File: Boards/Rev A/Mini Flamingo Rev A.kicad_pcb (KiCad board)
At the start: 2 copper layers, 38.1 x 25.4 mm, 23 parts, among them J1 ISP_Header, J2 APA102C Out, J3 Batt Conn, SW1 Power Switch, U1 ATTINY85-20SU, U2 APA102C

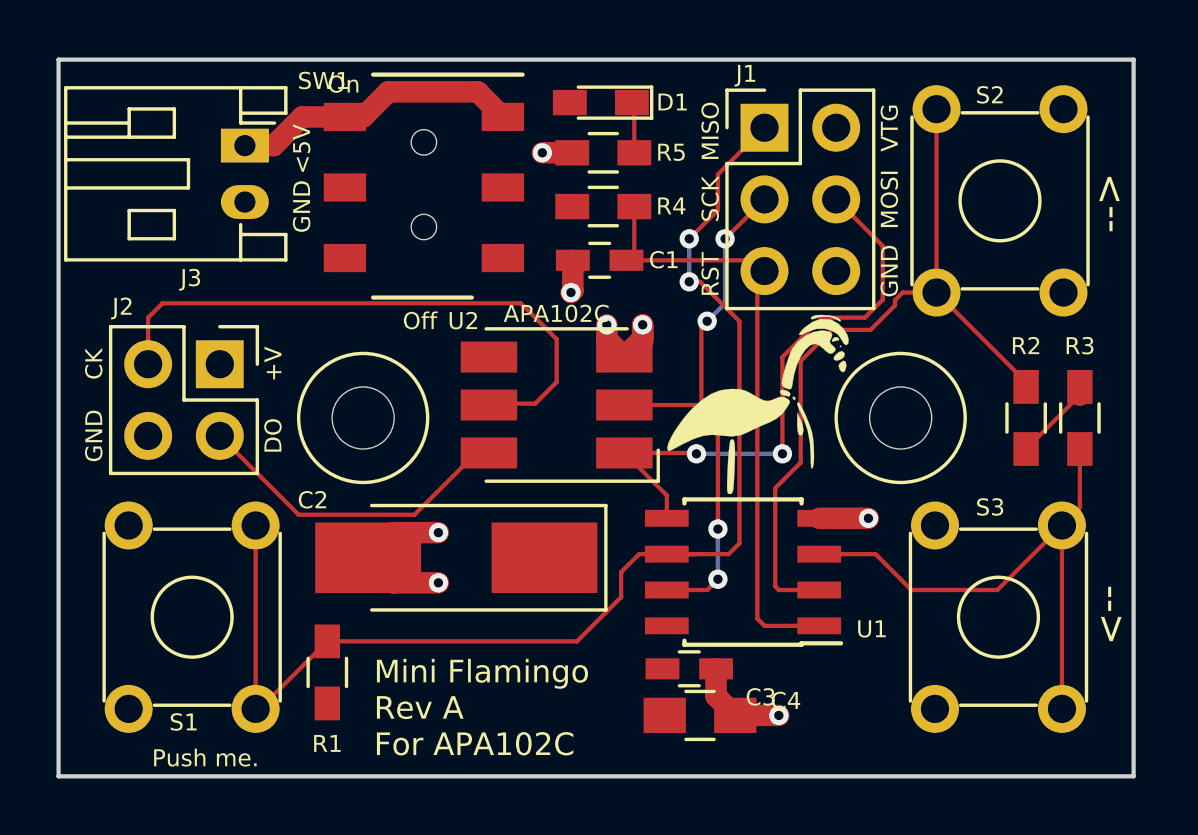
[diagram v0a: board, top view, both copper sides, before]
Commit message: Rev A final version as sent to fab
Had to change some parts so I could place the entire order on Digikey
(save for the APA102C).
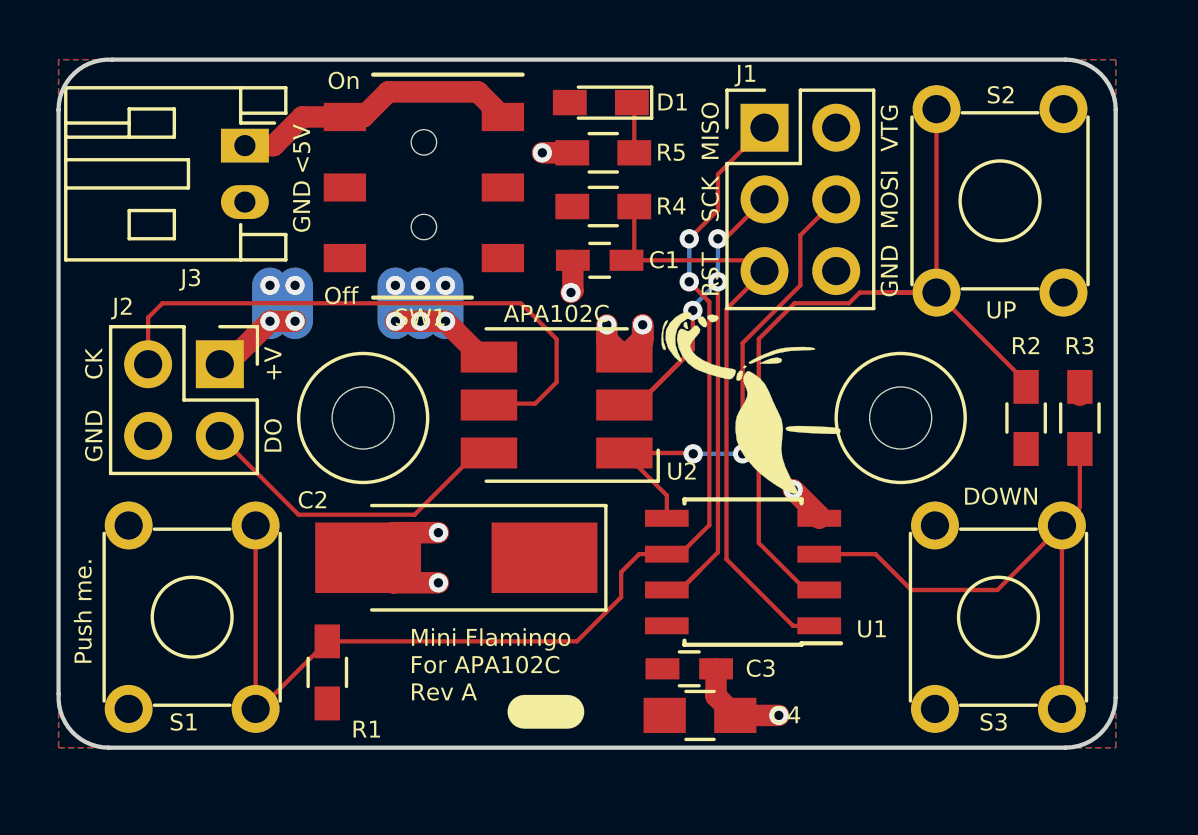
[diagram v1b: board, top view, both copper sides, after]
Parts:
- removed the G*** at (173.0, 88.5)
- added G***: LOGO, Project Footprints:flamingo_logo_25_38, B.Cu at (168.5, 87.5)
- moved G*** 0.80 mm to (174.9, 86.1), turned to 90 degrees
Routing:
- net +BATT: track 4.51 -> 15.5 mm, vias 0 -> 10
- net /SCK/WS2812Clock: track 19.3 -> 25.6 mm, vias 4 -> 3
- net /PIN2/SW2: track 27.1 -> 30.4 mm
- net /PIN6/SW1: track 44.6 -> 41.4 mm
- net /MOSI/WS2812Data: track 20.6 -> 17.5 mm
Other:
- board size 38.1 x 25.4 mm -> 37.5 x 24.4 mm
- board text added: "DOWN"
- board text added: "Mini Flamingo For APA102C Rev A"
- board text added: "Mini Flamingo Paul Blackburn 2018 GitHub: @individual61"
- board text added: "UP"
- board text removed: "-->"
- board text removed: "Mini Flamingo Rev A For APA102C"
- board text removed: "Mini Flamingo Rev A Mod Paul Blackburn 2018 GitHub: @individual61"
